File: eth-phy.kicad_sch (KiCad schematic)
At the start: 60 parts, among them J10 JST_SH_1x12_SM12B-SRSS-TB-LF-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, U2 TPD4E05U06QDQARQ1, U28 RTL8211FDI-CG, U29 TPD4E05U06QDQARQ1, Y5 Resonator_25MHz_445

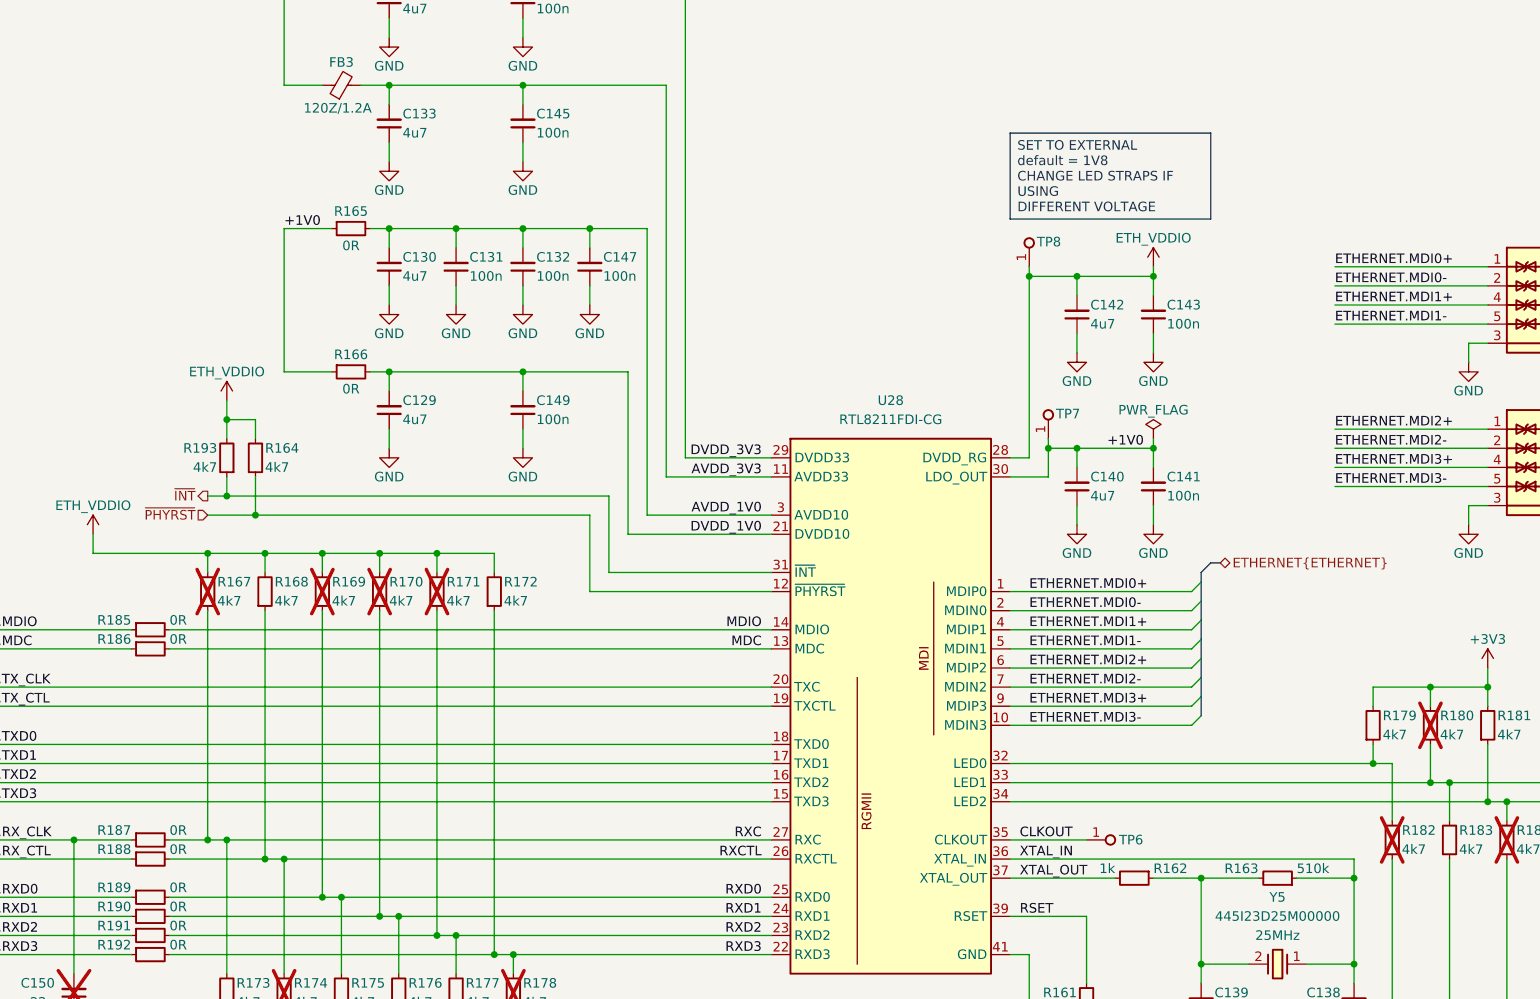
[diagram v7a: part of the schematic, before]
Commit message: [#83331] Added PECI circuitry. Small top fixes
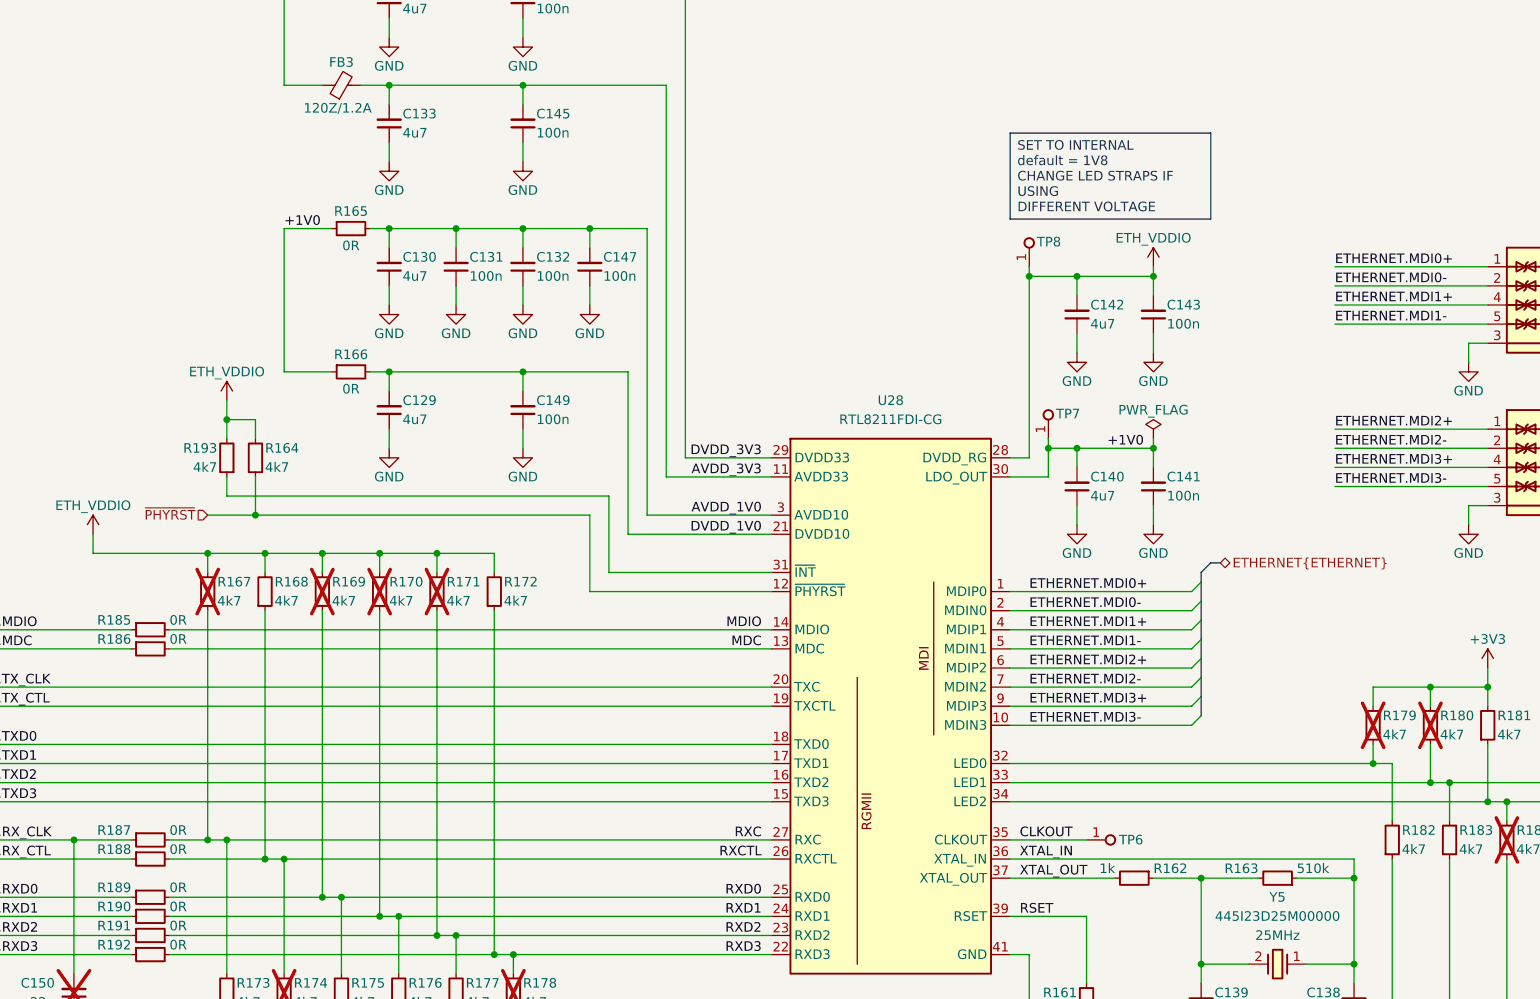
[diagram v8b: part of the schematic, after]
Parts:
- R179: now not fitted
- R182: now fitted
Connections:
- net ~{INT}: no longer names the net of R193.1, U28.31 (~{INT})
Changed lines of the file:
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@@
 		(rev "1.0.0")
 	)
-	(text_box "SET TO EXTERNAL\ndefault = 1V8\nCHANGE LED STRAPS IF USING\nDIFFERENT VOLTAGE"
+	(text_box "SET TO INTERNAL\ndefault = 1V8\nCHANGE LED STRAPS IF USING\nDIFFERENT VOLTAGE"
 		(exclude_from_sim no)
 		(at 226.06 90.17 0)
@@
 	)
 	(junction
-		(at 121.92 138.43)
-		(diameter 0)
-		(color 0 0 0 0)
-	)
-	(junction
 		(at 142.24 194.31)
 		(diameter 0)
@@
 	(wire
 		(pts
-			(xy 119.38 138.43) (xy 121.92 138.43)
-		)
-		(stroke
-			(width 0)
-			(type default)
-		)
-	)
-	(wire
-		(pts
 			(xy 292.1 179.07) (xy 298.45 179.07)
 		)
@@
 		)
 	)
-	(hierarchical_label "~{INT}"
-		(shape output)
-		(at 119.38 138.43 180)
-		(effects
-			(font
-				(size 1.27 1.27)
-			)
-			(justify right)
-		)
-	)
 	(hierarchical_label "ETH_LED_G"
 		(shape output)
@@
 		(in_bom yes)
 		(on_board yes)
-		(dnp yes)
+		(dnp no)
 		(property "Reference" "R182"
 			(at 278.13 182.88 90)
@@
 		(in_bom yes)
 		(on_board yes)
-		(dnp no)
+		(dnp yes)
 		(property "Reference" "R179"
 			(at 275.59 167.64 90)
